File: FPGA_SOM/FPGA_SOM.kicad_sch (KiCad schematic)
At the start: 47 parts, among them J102 Conn_01x14, J103 Conn_01x09, J104 Conn_01x11, J105 Conn_01x02, J106 Conn_01x06, U101 W25X20CLSN, U102 AP2127N-3.3, U104 AP2127N-1.2, U105 ICE40UP5K-SG48ITR, X101 ECS-2520MV-xxx-xx

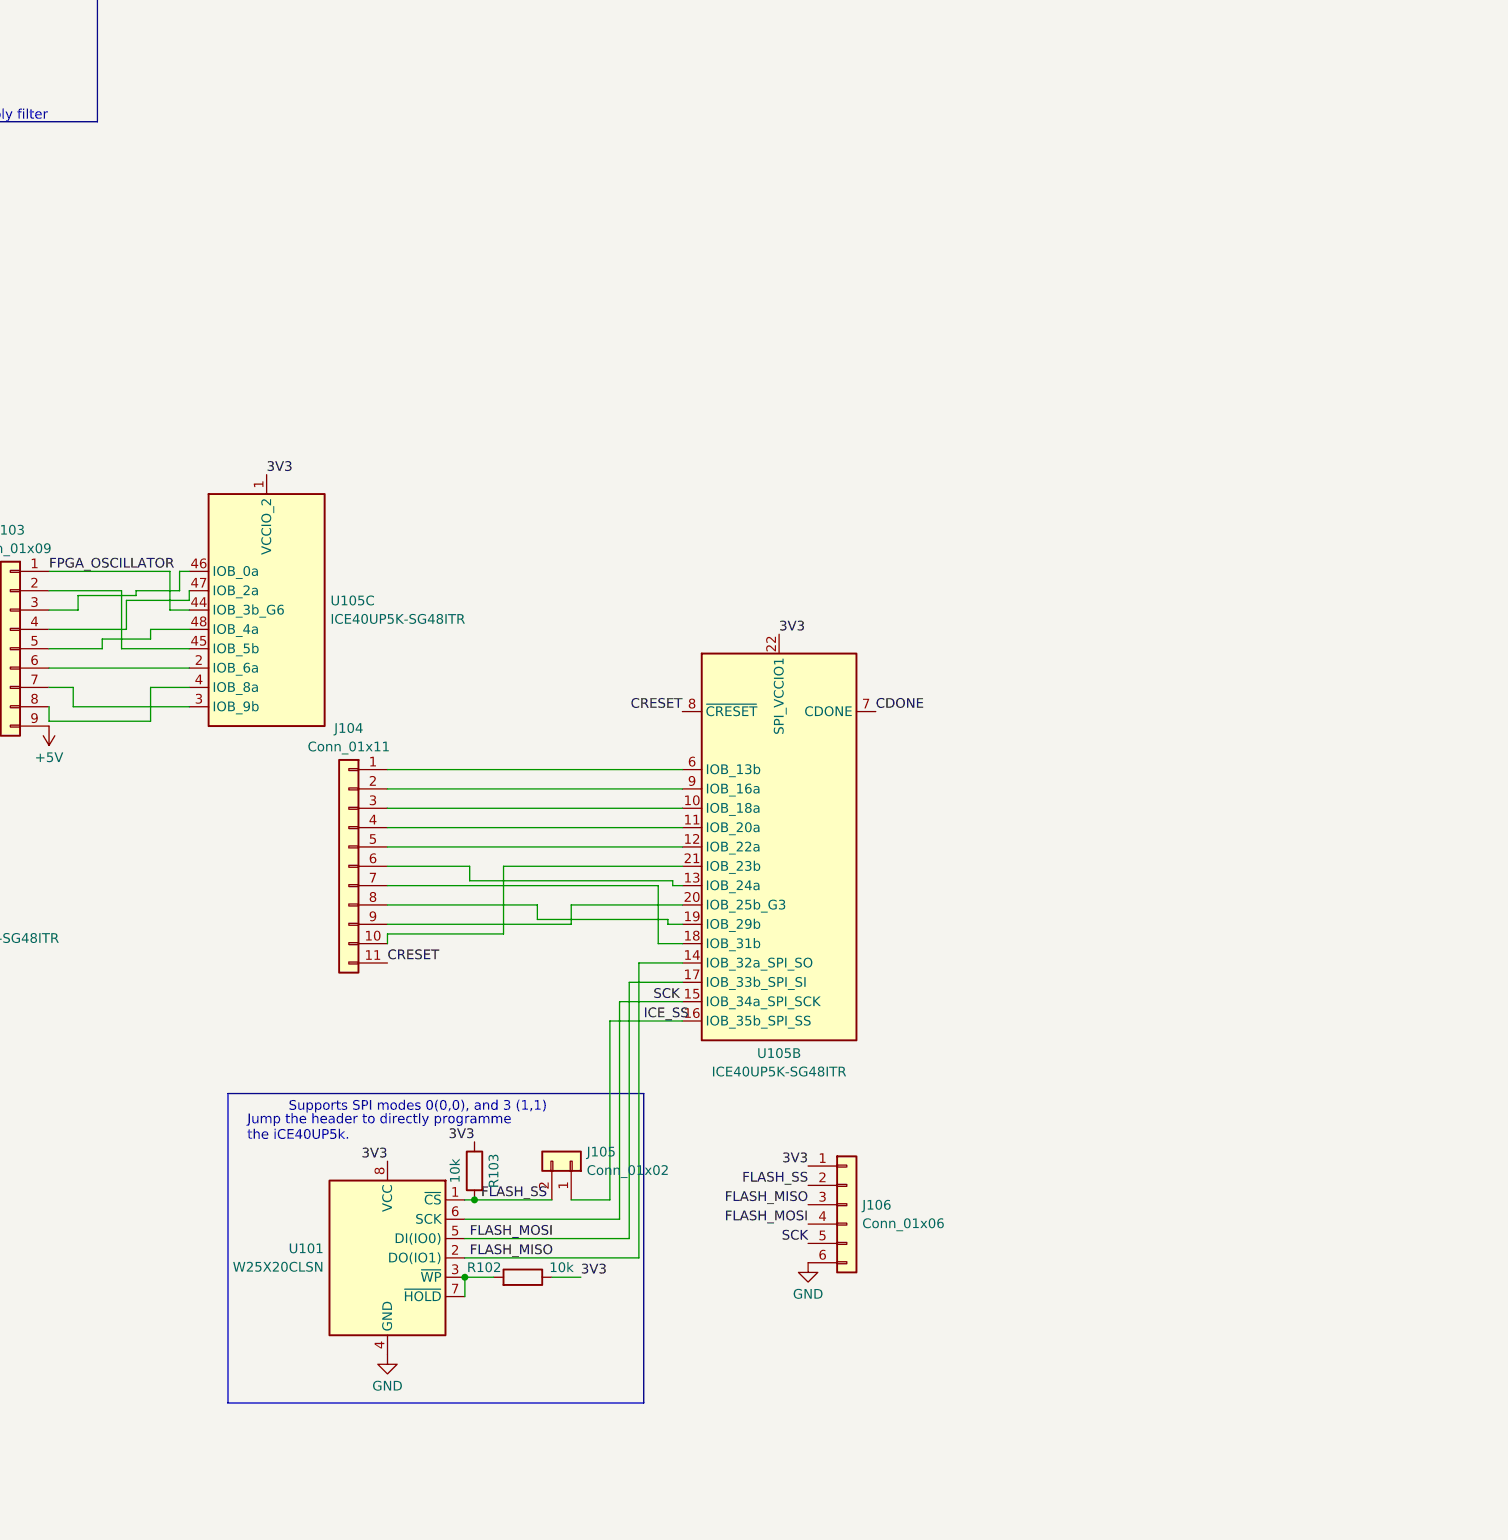
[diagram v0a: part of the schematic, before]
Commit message: Version one. Had some errors documented in schematic which I will fix in version 2.
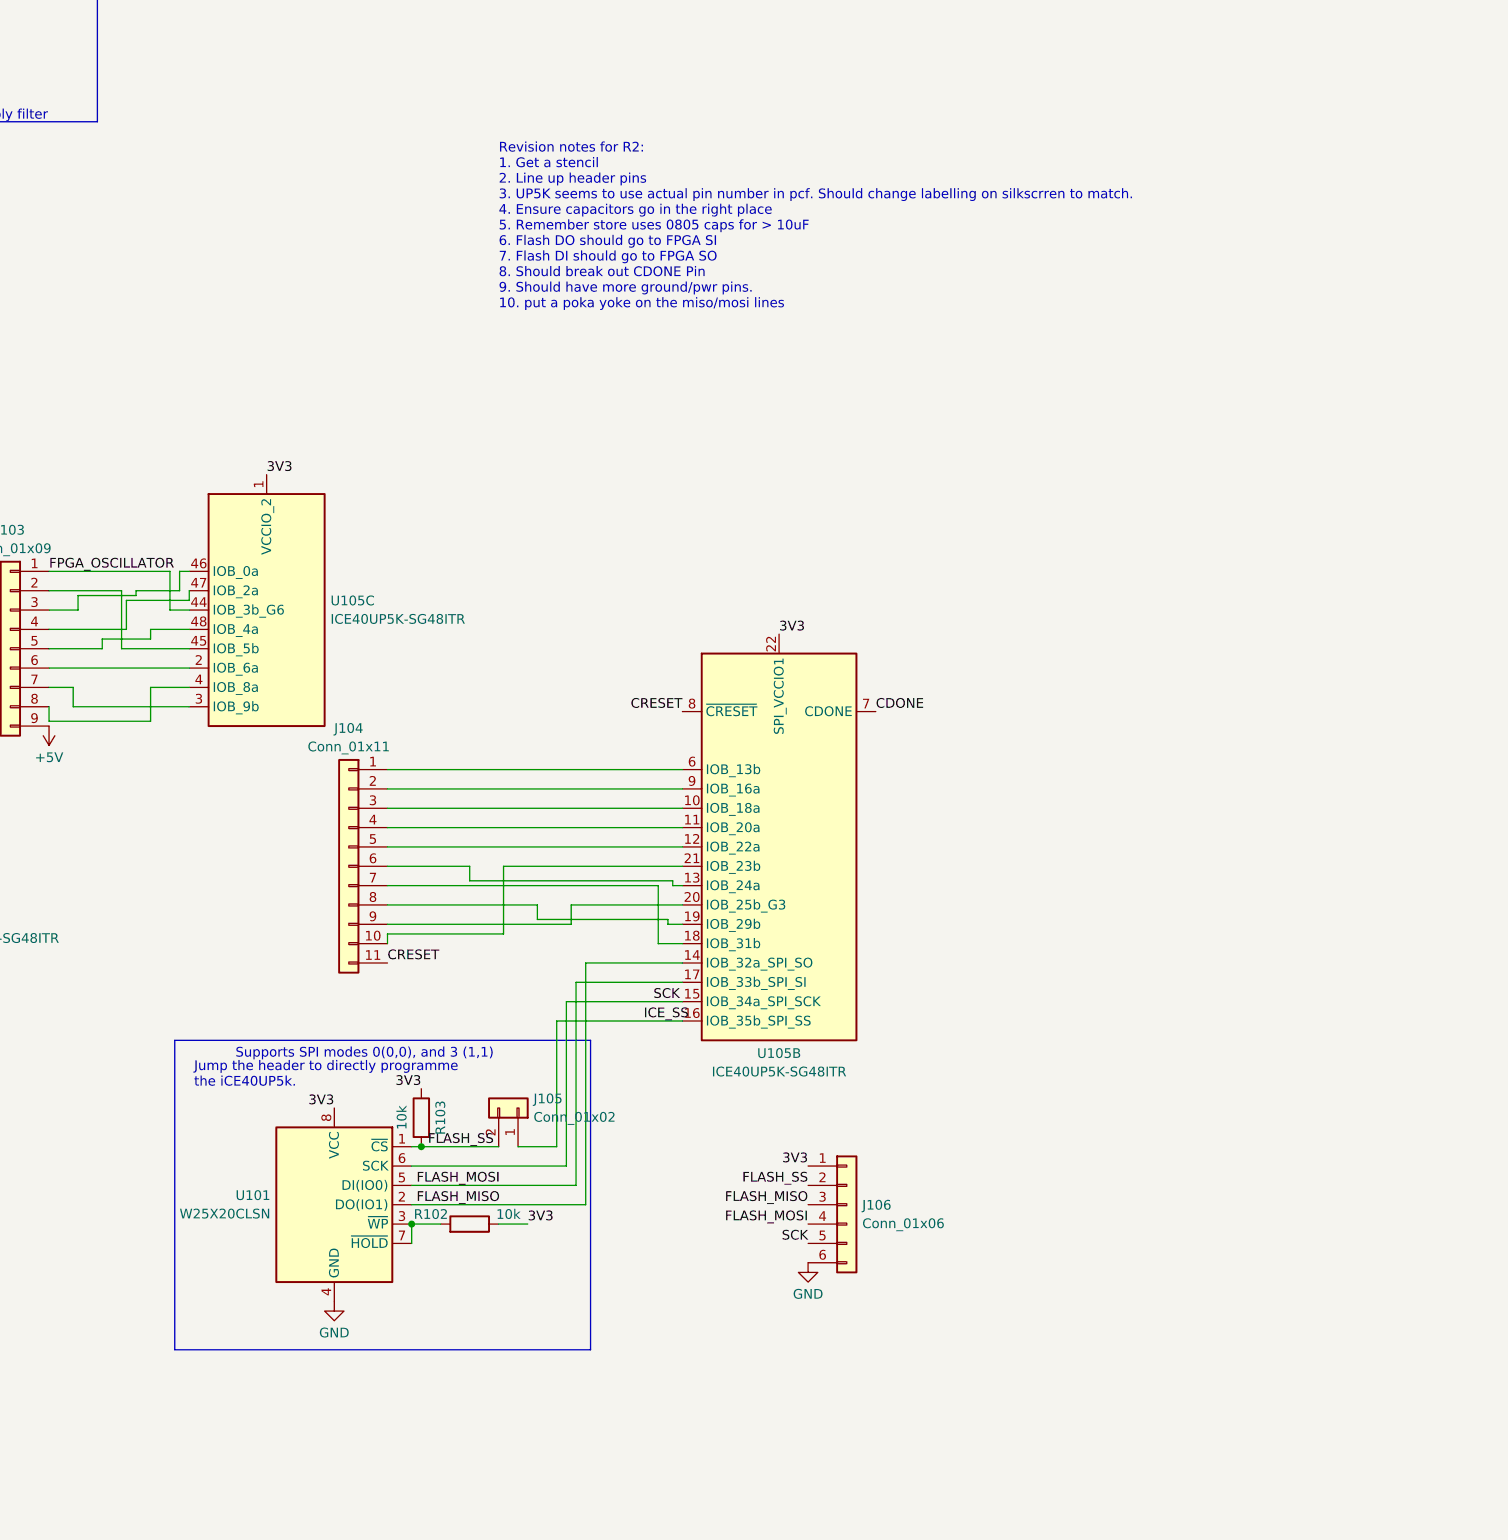
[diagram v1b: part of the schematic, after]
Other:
- note added: "Revision notes for R2: 1. Get a stencil 2. Line up header pins 3. UP5K seems to use actual pin number in pcf. Should change labelling on silkscrren to match. 4. Ensure capacitors go in the right place 5. Remember store uses 0805 caps for > 10uF 6. Flash DO should go to FPGA SI 7. Flash DI should go to FPGA SO 8. Should break out CDONE Pin 9. Should have more ground/pwr pins. 10. put a poka yoke o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"
- moved on the sheet: J105, R102, R103, U101

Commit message: First attempt at V2. Likely to be changed in the near future.
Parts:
- removed J106: Conn_01x06, Connector_PinHeader_2.54mm:PinHeader_1x06_P2.54mm_Vertical, symbol Connector_Generic:Conn_01x06
- added C133: 100n, Capacitor_SMD:C_0603_1608Metric, symbol Device:C
- added J4: Conn_01x04, Connector_PinHeader_2.54mm:PinHeader_1x04_P2.54mm_Vertical, symbol Connector_Generic:Conn_01x04
- added J6: Conn_02x04_Counter_Clockwise, Connector_PinHeader_2.54mm:PinHeader_2x04_P2.54mm_Vertical, symbol Connector_Generic:Conn_02x04_Counter_Clockwise
- added R103 (x2): 0, Resistor_SMD:R_0603_1608Metric, symbol Device:R
- added TP1, TP10, TP11, TP12, TP2, TP3, TP4, TP5, TP6, TP7, TP8, TP9: TestPoint, TestPoint:TestPoint_Pad_2.0x2.0mm, symbol Connector:TestPoint
- C101, C104, C107, C110, C120, C123, C126, C132, C133, C135, C136, C138, C143: footprint Capacitor_SMD:C_0603_1608Metric_Pad1.08x0.95mm_HandSolder -> Capacitor_SMD:C_0603_1608Metric
- C119, C122, C125, C131, C134, C137: footprint Capacitor_SMD:C_0603_1608Metric_Pad1.08x0.95mm_HandSolder -> Capacitor_SMD:C_0805_2012Metric
- D1: renamed from D104; footprint Diode_SMD:D_0603_1608Metric_Pad1.05x0.95mm_HandSolder -> Diode_SMD:D_0603_1608Metric
- D101, D102, D103: footprint Diode_SMD:D_0603_1608Metric_Pad1.05x0.95mm_HandSolder -> Diode_SMD:D_0603_1608Metric
- FB1: renamed from FB101; footprint Resistor_SMD:R_0805_2012Metric_Pad1.20x1.40mm_HandSolder -> Resistor_SMD:R_1206_3216Metric
- R102, R103, R108, R109, R111, R112: footprint Resistor_SMD:R_0603_1608Metric_Pad0.98x0.95mm_HandSolder -> Resistor_SMD:R_0603_1608Metric
- R113: value 5k -> 4k7; footprint Resistor_SMD:R_0603_1608Metric_Pad0.98x0.95mm_HandSolder -> Resistor_SMD:R_0603_1608Metric
- R3: renamed from R114; footprint Resistor_SMD:R_0603_1608Metric_Pad0.98x0.95mm_HandSolder -> Resistor_SMD:R_0603_1608Metric
- R4: renamed from R111; footprint Resistor_SMD:R_0603_1608Metric_Pad0.98x0.95mm_HandSolder -> Resistor_SMD:R_0603_1608Metric
- R5: renamed from R107; footprint Resistor_SMD:R_0603_1608Metric_Pad0.98x0.95mm_HandSolder -> Resistor_SMD:R_0603_1608Metric
- renumbered D106 to D2, D105 to D3, D108 to D4, J102 to J1, J103 to J2, J104 to J3, J105 to J5, U105 to U1, U102 to U2, U104 to U3
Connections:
- net +5V: now also J4.1 (Pin_1)
- net 1V2: now also J4.3 (Pin_3), TP4.1
- net 3V3: now also C133.1, J4.2 (Pin_2), J6.6 (Pin_6), TP3.1
- net CDONE: now also J6.7 (Pin_7), TP11.1
- net CRESET: now also J3.1 (Pin_1), J6.8 (Pin_8), TP10.1; no longer J3.11 (Pin_11)
- net FLASH_MISO: now also U1.17 (IOB_33b_SPI_SI), R103.1, TP9.1; no longer U1.14 (IOB_32a_SPI_SO)
- net FLASH_MOSI: now also U1.14 (IOB_32a_SPI_SO), R103.1, TP8.1; no longer U1.17 (IOB_33b_SPI_SI)
- net FLASH_SS: now also J6.1 (Pin_1), TP5.1
- net FPGA_OSCILLATOR: now also TP12.1
- net GND: now also C133.2, J4.4 (Pin_4), J6.5 (Pin_5)
- net ICE_SS: now also TP6.1
- net SCK: now also J6.4 (Pin_4), TP7.1
- net VCCPLL: now also TP2.1
- net at U1.6 (IOB_13b): now also J3.2 (Pin_2); no longer J3.1 (Pin_1)
- net at J3.10 (Pin_10): now also U1.20 (IOB_25b_G3); no longer U1.21 (IOB_23b)
- net at U1.9 (IOB_16a): now also J3.3 (Pin_3); no longer J3.2 (Pin_2)
- net at U1.10 (IOB_18a): now also J3.4 (Pin_4); no longer J3.3 (Pin_3)
- net at U1.11 (IOB_20a): now also J3.5 (Pin_5); no longer J3.4 (Pin_4)
- net at U1.12 (IOB_22a): now also J3.6 (Pin_6); no longer J3.5 (Pin_5)
- net at U1.13 (IOB_24a): now also J3.7 (Pin_7); no longer J3.6 (Pin_6)
- net at U1.18 (IOB_31b): now also J3.8 (Pin_8); no longer J3.7 (Pin_7)
- net at U1.19 (IOB_29b): now also J3.9 (Pin_9); no longer J3.8 (Pin_8)
- net at R5.2: now also U1.39 (RGB0); no longer U1.41 (RGB2)
- net at R3.2: now also U1.41 (RGB2); no longer U1.39 (RGB0)
- net at U1.42 (IOT_51a): now also J1.13 (Pin_13); no longer J1.14 (Pin_14)
- net at U1.43 (IOT_49a): now also J1.14 (Pin_14); no longer J1.13 (Pin_13)
- net at D1.1 (K), U1.24 (VPP_2V5): now also TP1.1
- new net: J3.11 (Pin_11), U1.21 (IOB_23b)
- new net: J6.3 (Pin_3), R103.2
- new net: J6.2 (Pin_2), R103.2
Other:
- note added: "Pokayoke"
- moved on the sheet: D2, D4, J3, R3, R4, R5

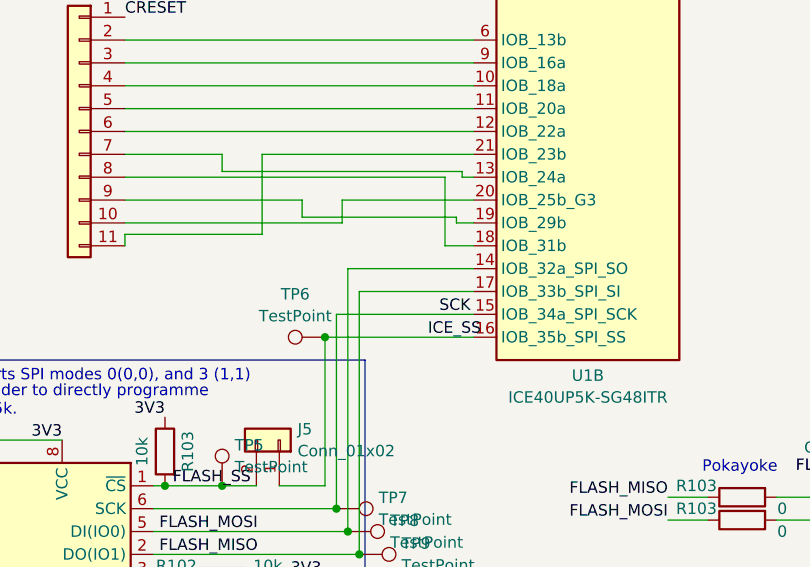
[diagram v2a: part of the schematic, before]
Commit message: add pullup resistor to sck on schematic.
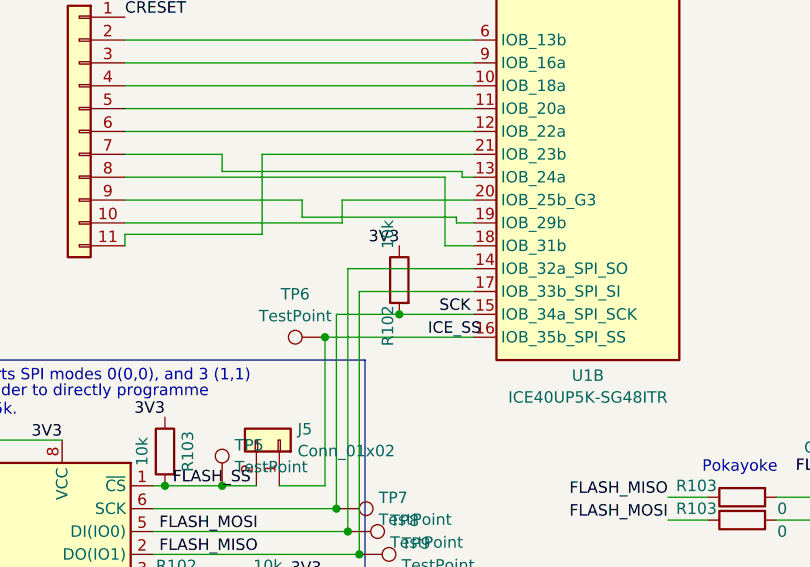
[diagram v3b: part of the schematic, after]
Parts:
- added R102: 10k, Resistor_SMD:R_0603_1608Metric, symbol Device:R
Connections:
- net 3V3: now also R102.1
- net SCK: now also R102.2
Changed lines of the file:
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@@
   (junction (at 107.95 73.025) (diameter 0) (color 0 0 0 0)
   )
+  (junction (at 284.48 186.055) (diameter 0) (color 0 0 0 0)
+  )
   (junction (at 135.255 231.14) (diameter 0) (color 0 0 0 0)
   )
@@
     (stroke (width 0) (type default))
   )
-  (wire (pts (xy 277.495 186.055) (xy 292.735 186.055))
+  (wire (pts (xy 277.495 186.055) (xy 284.48 186.055))
     (stroke (width 0) (type default))
   )
@@
   )
   (wire (pts (xy 149.86 65.405) (xy 158.75 65.405))
+    (stroke (width 0) (type default))
+  )
+  (wire (pts (xy 284.48 186.055) (xy 292.735 186.055))
     (stroke (width 0) (type default))
   )
@@
   (label "ICE_SS" (at 287.655 188.595 0) (fields_autoplaced)
     (effects (font (size 1.27 1.27)) (justify left bottom))
+  )
+  (label "3V3" (at 284.48 178.435 180) (fields_autoplaced)
+    (effects (font (size 1.27 1.27)) (justify right bottom))
   )
   (label "3V3" (at 258.445 250.825 180) (fields_autoplaced)
@@
         )
       )
+    )
+  )
+  (symbol (lib_id "Device:R") (at 284.48 182.245 0) (mirror y) (unit 1)
+    (in_bom yes) (on_board yes) (dnp no)
+    (property "Reference" "R102" (at 283.21 187.325 90)
+      (effects (font (size 1.27 1.27)))
+    )
+    (property "Value" "10k" (at 283.21 177.165 90)
+      (effects (font (size 1.27 1.27)))
+    )
+    (property "Footprint" "Resistor_SMD:R_0603_1608Metric" (at 286.258 182.245 90)
+      (effects (font (size 1.27 1.27)) hide)
+    )
+    (property "Datasheet" "https://www.digikey.co.nz/en/products/detail/yageo/AC0603FR-1310KL/13694194" (at 284.48 182.245 0)
+      (effects (font (size 1.27 1.27)) hide)
+    )
+    (property "Price" "" (at 284.48 182.245 0)
+      (effects (font (size 1.27 1.27)) hide)
+    )
+    (pin "1")
+    (pin "2")
+    (instances
+      (project "ICE40Breakout"
+        (path "/7a8e4b43-2524-4863-bf7c-adf3dbbc9623"
+          (reference "R102") (unit 1)
+        )
+      )
+      (project "FPGA_SOM"
+        (path "/c9513ae4-ec90-4b73-ae24-d135d02c4e68"
+          (reference "R13") (unit 1)
+        )
+      )
